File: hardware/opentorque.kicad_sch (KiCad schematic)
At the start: 0 parts

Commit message: Arrange components
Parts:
- added GND1, VCC_12-56: TestPoint, TestPoint:TestPoint_Pad_4.0x4.0mm, symbol Connector:TestPoint
- added R17: 20k, Resistor_SMD:R_0603_1608Metric, symbol Device:R
- added R18: 1k, Resistor_SMD:R_0603_1608Metric, symbol Device:R
- added U10: AMS1117-5.0_C347223, easyeda2kicad:SOT-223_L6.7-W3.5-P2.30-BR, symbol easyeda2kicad:AMS1117-5.0_C347223
- added U11: AMS1117-3.3_C347222, easyeda2kicad:SOT-223-4_L6.5-W3.5-P2.30-LS7.0-BR, symbol easyeda2kicad:AMS1117-3.3_C347222
- added U9: UMW78M12, easyeda2kicad:TO-252-2_L6.6-W6.1-P4.57-LS9.9-BR-CW, symbol easyeda2kicad:UMW78M12
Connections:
- new net: R17.2, R18.1
- new net +12V: U10.3 (VIN), U9.3 (OUT)
- new net +3.3V: U11.2 (VOUT(TAB)), U11.4 (TAB)
- new net +5V: U10.2 (VOUT(TAB)), U10.4 (TAB), U11.3 (VIN)
- new net GND: GND1.1, R18.2, U10.1 (ADJ(GND)), U11.1 (ADJ(GND)), U9.2 (GND)
- new net VCC: R17.1, U9.1 (IN), VCC_12-56.1
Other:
- sheet phasedriver renamed phasedriver U
- added sheet phasedriver V (schematics/phasedriver.kicad_sch)
- added sheet phasedriver W (schematics/phasedriver.kicad_sch)
- sheet phasedriver U ports: added 5V, AOUT; removed phase
- sheet rp2040 ports: added 3.3V, 5V, GND, GPIO0, GPIO1, GPIO2, GPIO26, GPIO27, GPIO28, GPIO29, GPIO3, GPIO4, GPIO5; removed none
- note added: "VCC ADC configured to read up to 66V"

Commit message: Add more routing
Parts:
- removed U10: AMS1117-5.0_C347223, easyeda2kicad:SOT-223_L6.7-W3.5-P2.30-BR, symbol easyeda2kicad:AMS1117-5.0_C347223
- added C28: 100n, Capacitor_SMD:C_0603_1608Metric, symbol Device:C
- added U10: AS5600-ASOT, easyeda2kicad:SOIC-8_L5.0-W4.0-P1.27-LS6.0-BL, symbol easyeda2kicad:AS5600-ASOT
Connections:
- net +5V is gone; now on net +12V: U11.3 (VIN)
- net GND: now also C28.2, U10.4 (GND), U10.5 (PGO)
- net +3.3V renamed +3V3
- net +3V3: now also C28.1, U10.1 (VDD5V), U10.2 (VDD3V3)
- no-connect marks 0 -> 2
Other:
- sheet phasedriver U ports: added +3V3; removed 5V
- sheet phasedriver V ports: added +3V3; removed 5V
- sheet phasedriver W ports: added +3V3; removed 5V
- sheet rp2040 ports: added GPIO10, GPIO11, GPIO18, GPIO19, GPIO20, GPIO21; removed GPIO0, GPIO1, GPIO2, GPIO3, GPIO4, GPIO5

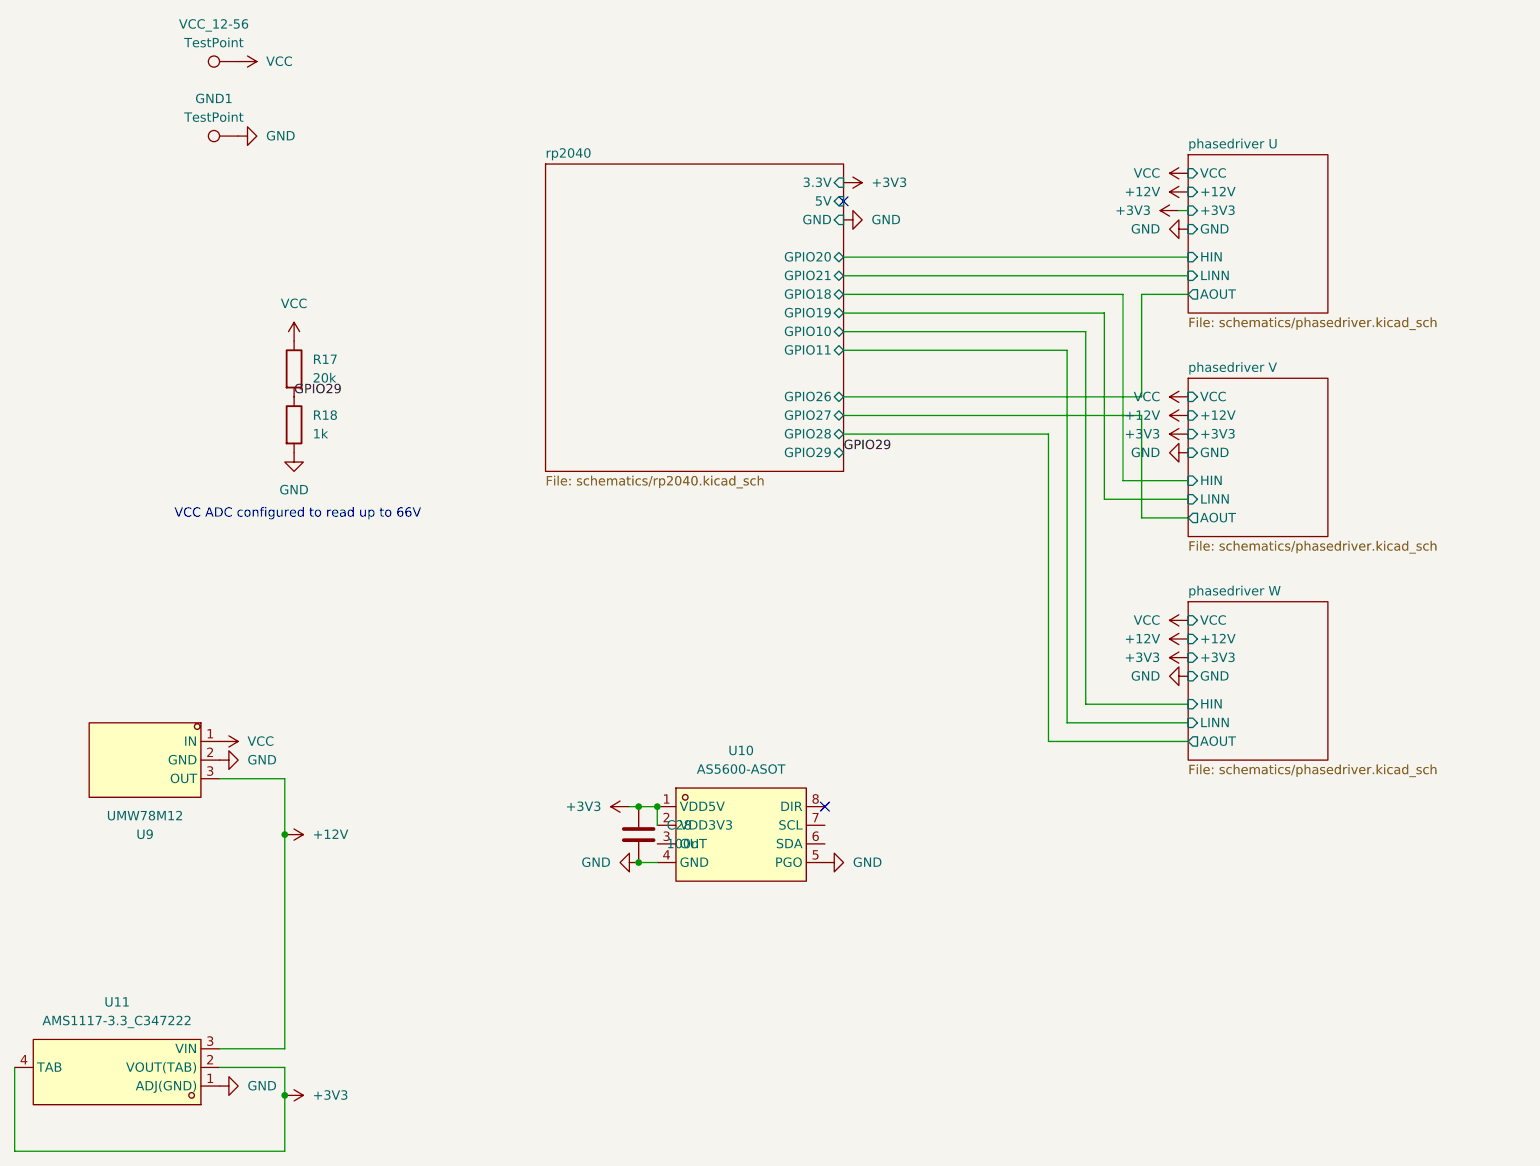
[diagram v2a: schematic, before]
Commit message: Fix BOOTSEL resistors and add reset button
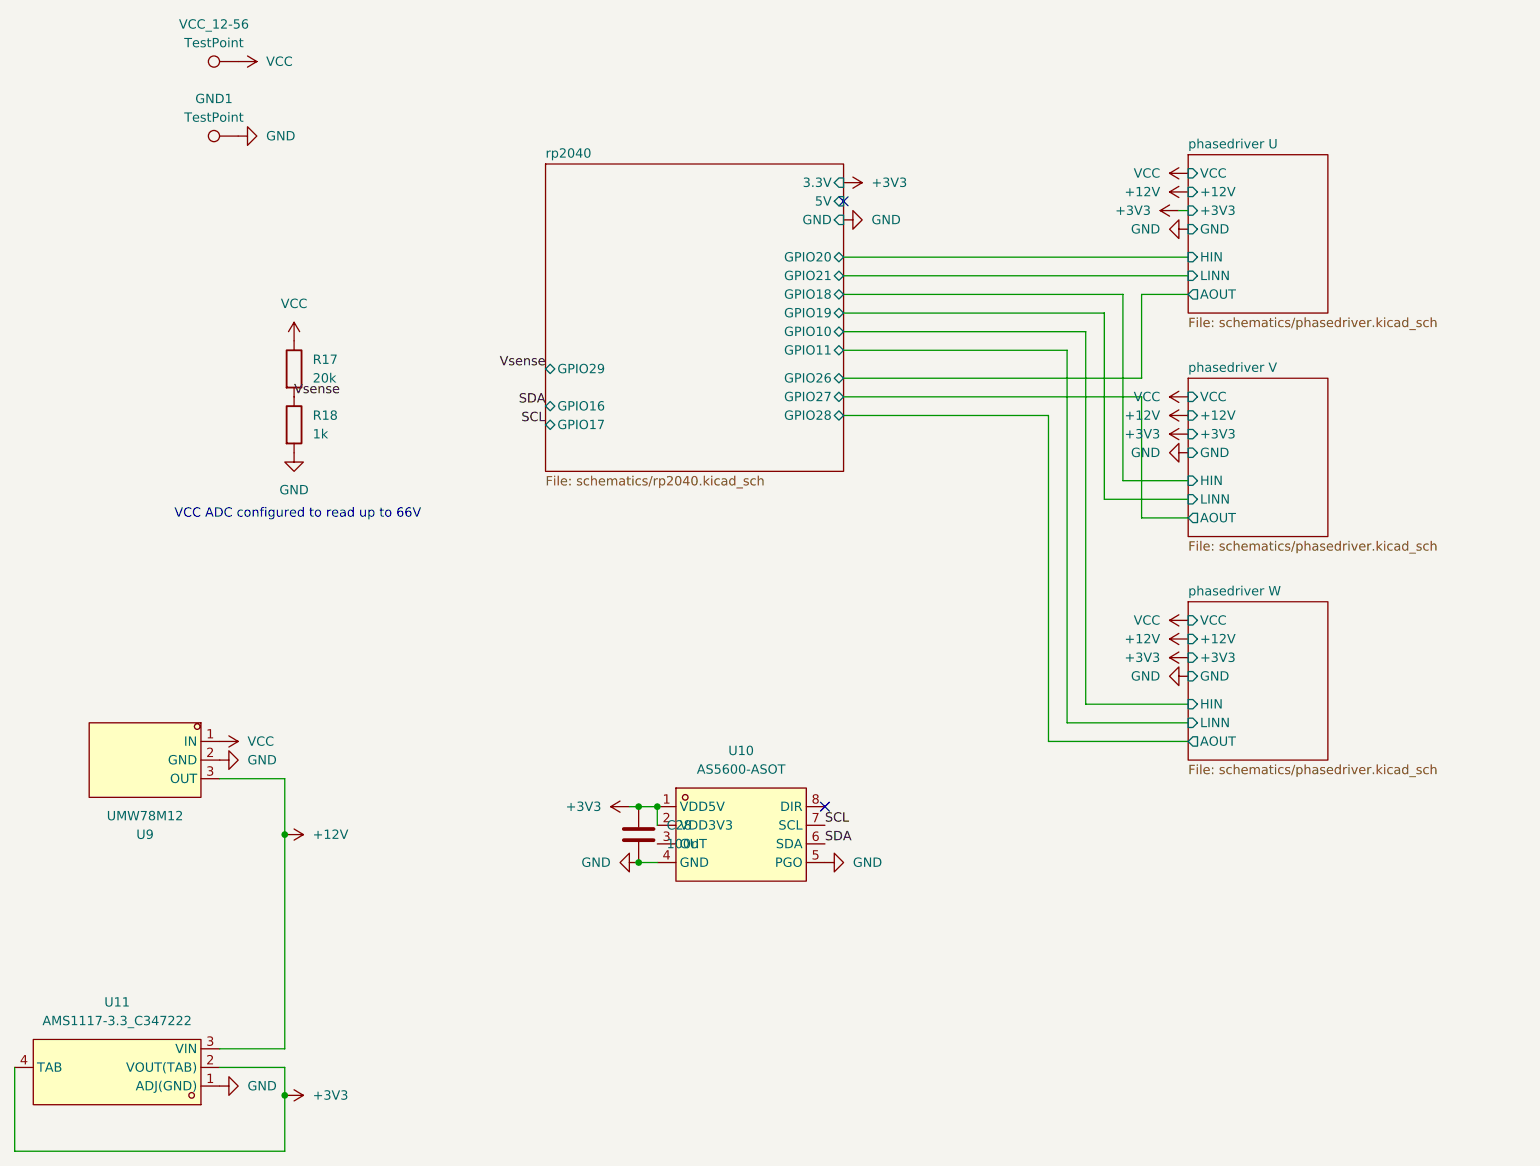
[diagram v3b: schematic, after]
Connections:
- net Vsense: now reaches R17.2, R18.1
- net SDA: now reaches U10.6 (SDA)
- net SCL: now reaches U10.7 (SCL)
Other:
- sheet rp2040 ports: added GPIO16, GPIO17; removed none
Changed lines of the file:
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@@
 	(wire
 		(pts
-			(xy 186.69 52.07) (xy 186.69 66.04)
+			(xy 186.69 52.07) (xy 186.69 63.5)
 		)
 		(stroke
@@
 	(wire
 		(pts
-			(xy 186.69 82.55) (xy 186.69 68.58)
+			(xy 186.69 82.55) (xy 186.69 66.04)
 		)
 		(stroke
@@
 	(wire
 		(pts
-			(xy 173.99 113.03) (xy 173.99 71.12)
+			(xy 173.99 113.03) (xy 173.99 68.58)
 		)
 		(stroke
@@
 	(wire
 		(pts
-			(xy 146.05 68.58) (xy 186.69 68.58)
+			(xy 146.05 66.04) (xy 186.69 66.04)
 		)
 		(stroke
@@
 	(wire
 		(pts
-			(xy 173.99 71.12) (xy 146.05 71.12)
+			(xy 173.99 68.58) (xy 146.05 68.58)
 		)
 		(stroke
@@
 	(wire
 		(pts
-			(xy 186.69 66.04) (xy 146.05 66.04)
+			(xy 186.69 63.5) (xy 146.05 63.5)
 		)
 		(stroke
@@
 		)
 	)
+	(label "SCL"
+		(at 143.51 124.46 0)
+		(effects
+			(font
+				(size 1.27 1.27)
+			)
+			(justify left bottom)
+		)
+	)
 	(label ""
 		(at 146.05 73.66 0)
@@
 		)
 	)
-	(label "GPIO29"
+	(label "Vsense"
 		(at 71.12 66.04 0)
 		(effects
@@
 		)
 	)
-	(label "GPIO29"
-		(at 146.05 73.66 0)
+	(label "SCL"
+		(at 105.41 69.85 180)
+		(effects
+			(font
+				(size 1.27 1.27)
+			)
+			(justify right bottom)
+		)
+	)
+	(label "SDA"
+		(at 105.41 67.31 180)
+		(effects
+			(font
+				(size 1.27 1.27)
+			)
+			(justify right bottom)
+		)
+	)
+	(label "Vsense"
+		(at 105.41 62.23 180)
+		(effects
+			(font
+				(size 1.27 1.27)
+			)
+			(justify right bottom)
+		)
+	)
+	(label "SDA"
+		(at 143.51 127 0)
 		(effects
 			(font
@@
 		)
 		(pin "GPIO26" bidirectional
-			(at 146.05 66.04 0)
+			(at 146.05 63.5 0)
 			(effects
 				(font
@@
 		)
 		(pin "GPIO27" bidirectional
-			(at 146.05 68.58 0)
+			(at 146.05 66.04 0)
 			(effects
 				(font
@@
 		)
 		(pin "GPIO28" bidirectional
-			(at 146.05 71.12 0)
+			(at 146.05 68.58 0)
 			(effects
 				(font
@@
 		)
 		(pin "GPIO29" bidirectional
-			(at 146.05 73.66 0)
+			(at 105.41 62.23 180)
 			(effects
 				(font
 					(size 1.27 1.27)
 				)
-				(justify right)
+				(justify left)
 			)
 		)
@@
 			)
 		)
+		(pin "GPIO16" bidirectional
+			(at 105.41 67.31 180)
+			(effects
+				(font
+					(size 1.27 1.27)
+				)
+				(justify left)
+			)
+		)
+		(pin "GPIO17" bidirectional
+			(at 105.41 69.85 180)
+			(effects
+				(font
+					(size 1.27 1.27)
+				)
+				(justify left)
+			)
+		)

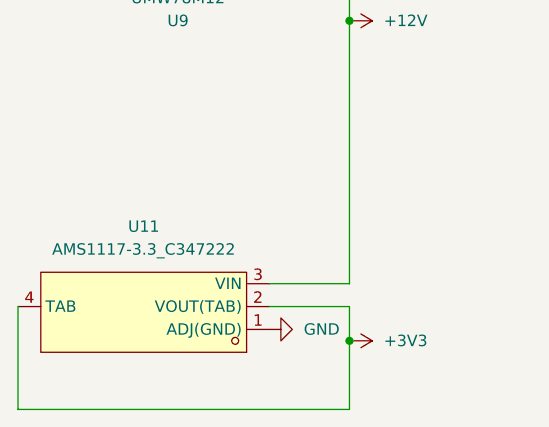
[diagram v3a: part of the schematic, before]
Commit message: Change logic supply to come from VBUS
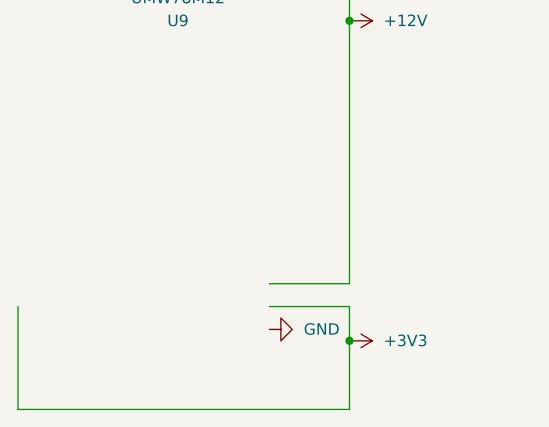
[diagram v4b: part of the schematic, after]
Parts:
- removed U11: AMS1117-3.3_C347222, easyeda2kicad:SOT-223-4_L6.5-W3.5-P2.30-LS7.0-BR, symbol easyeda2kicad:AMS1117-3.3_C347222
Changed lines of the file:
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@@
-	)
-	(symbol
-		(lib_id "easyeda2kicad:AMS1117-3.3_C347222")
-		(at 45.72 157.48 180)
-		(unit 1)
-		(exclude_from_sim no)
-		(in_bom yes)
-		(on_board yes)
-		(dnp no)
-		(fields_autoplaced yes)
-		(property "Reference" "U11"
-			(at 46.99 148.59 0)
-			(effects
-				(font
-					(size 1.27 1.27)
-				)
-			)
-		)
-		(property "Value" "AMS1117-3.3_C347222"
-			(at 46.99 151.13 0)
-			(effects
-				(font
-					(size 1.27 1.27)
-				)
-			)
-		)
-		(property "Footprint" "easyeda2kicad:SOT-223-4_L6.5-W3.5-P2.30-LS7.0-BR"
-			(at 45.72 147.32 0)
-			(effects
-				(font
-					(size 1.27 1.27)
-				)
-				(hide yes)
-			)
-		)
-		(property "Datasheet" "https://lcsc.com/product-detail/Others_Youtai-Semiconductor-Co-Ltd-AMS1117-3-3_C347222.html"
-			(at 45.72 144.78 0)
-			(effects
-				(font
-					(size 1.27 1.27)
-				)
-				(hide yes)
-			)
-		)
-		(property "Description" ""
-			(at 45.72 157.48 0)
-			(effects
-				(font
-					(size 1.27 1.27)
-				)
-				(hide yes)
-			)
-		)
-		(property "LCSC Part" "C347222"
-			(at 45.72 142.24 0)
-			(effects
-				(font
-					(size 1.27 1.27)
-				)
-				(hide yes)
-			)
-		)
-		(pin "4"
-		)
-		(pin "3"
-		)
-		(pin "2"
-		)
-		(pin "1"
-		)
-		(instances
-			(project ""
-				(path "/156c9497-a769-4db4-8dbf-f14841e5fc52"
-					(reference "U11")
-					(unit 1)
-				)
-			)
-		)
 	)
 	(symbol
